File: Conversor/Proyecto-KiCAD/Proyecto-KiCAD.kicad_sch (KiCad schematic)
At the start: 41 parts, among them Q1 IRFP150, Q2 IRFP150, Q3 IRFP150, Q4 IRFP150, U1 UCC21540, U2 UCC21540

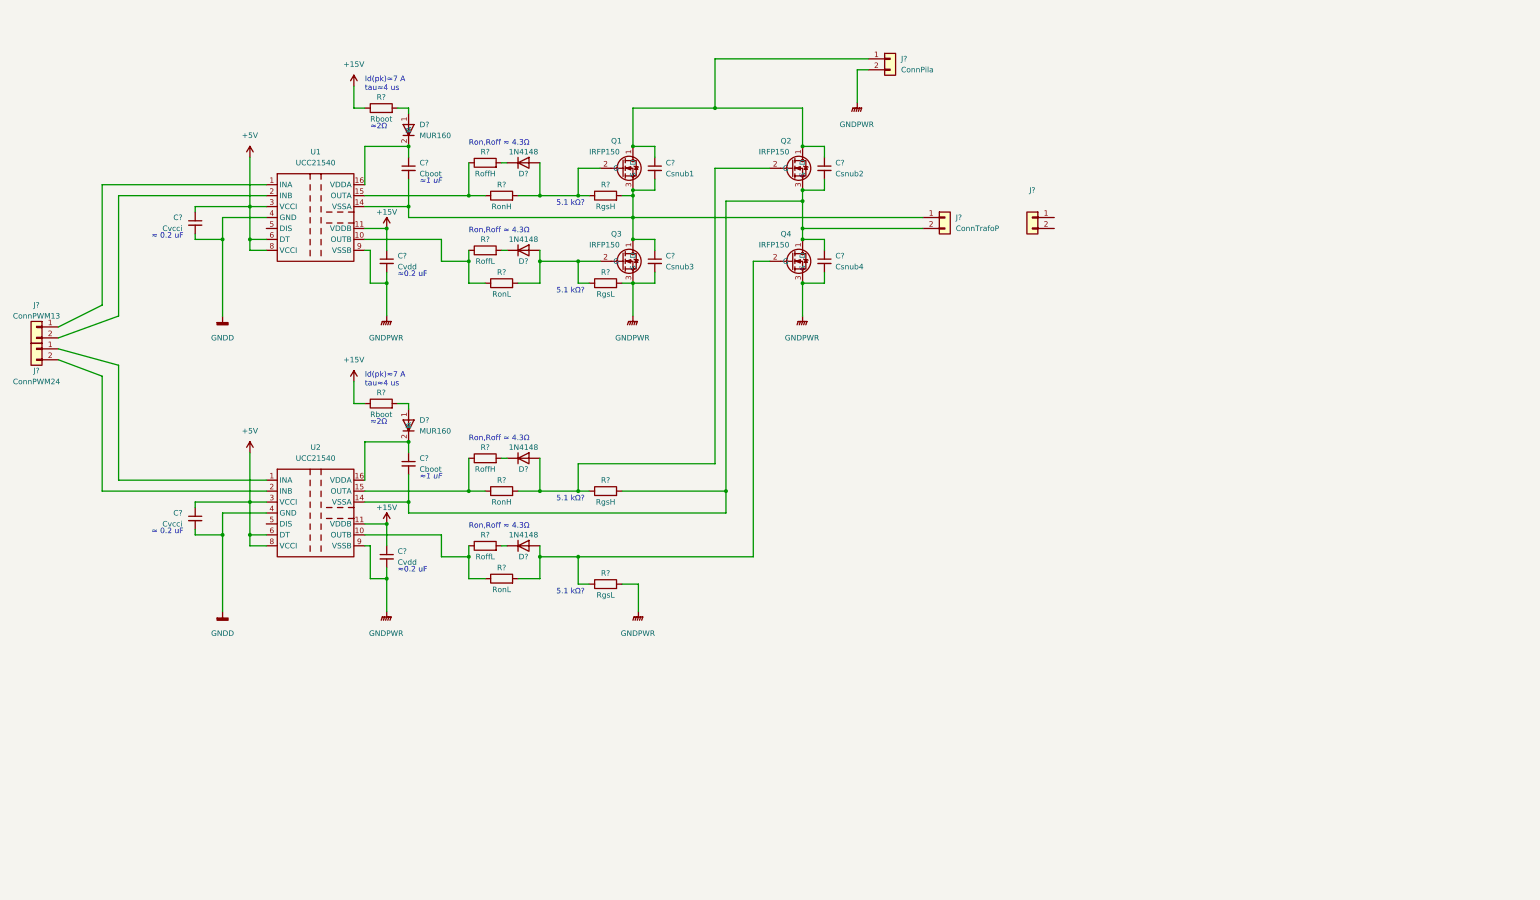
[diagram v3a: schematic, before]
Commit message: Terminar el esquematico del conversor
- Arrancado el esquematico de los sensores de tension/corriente/potencia
- Agregado el sensor Hall (ACS709) a la biblioteca de KiCAD y su datasheet
- Agregada datasheet de diodos MUR860 y SF86
- Mandado mail a Elemon consultando stock de diodos y transistores
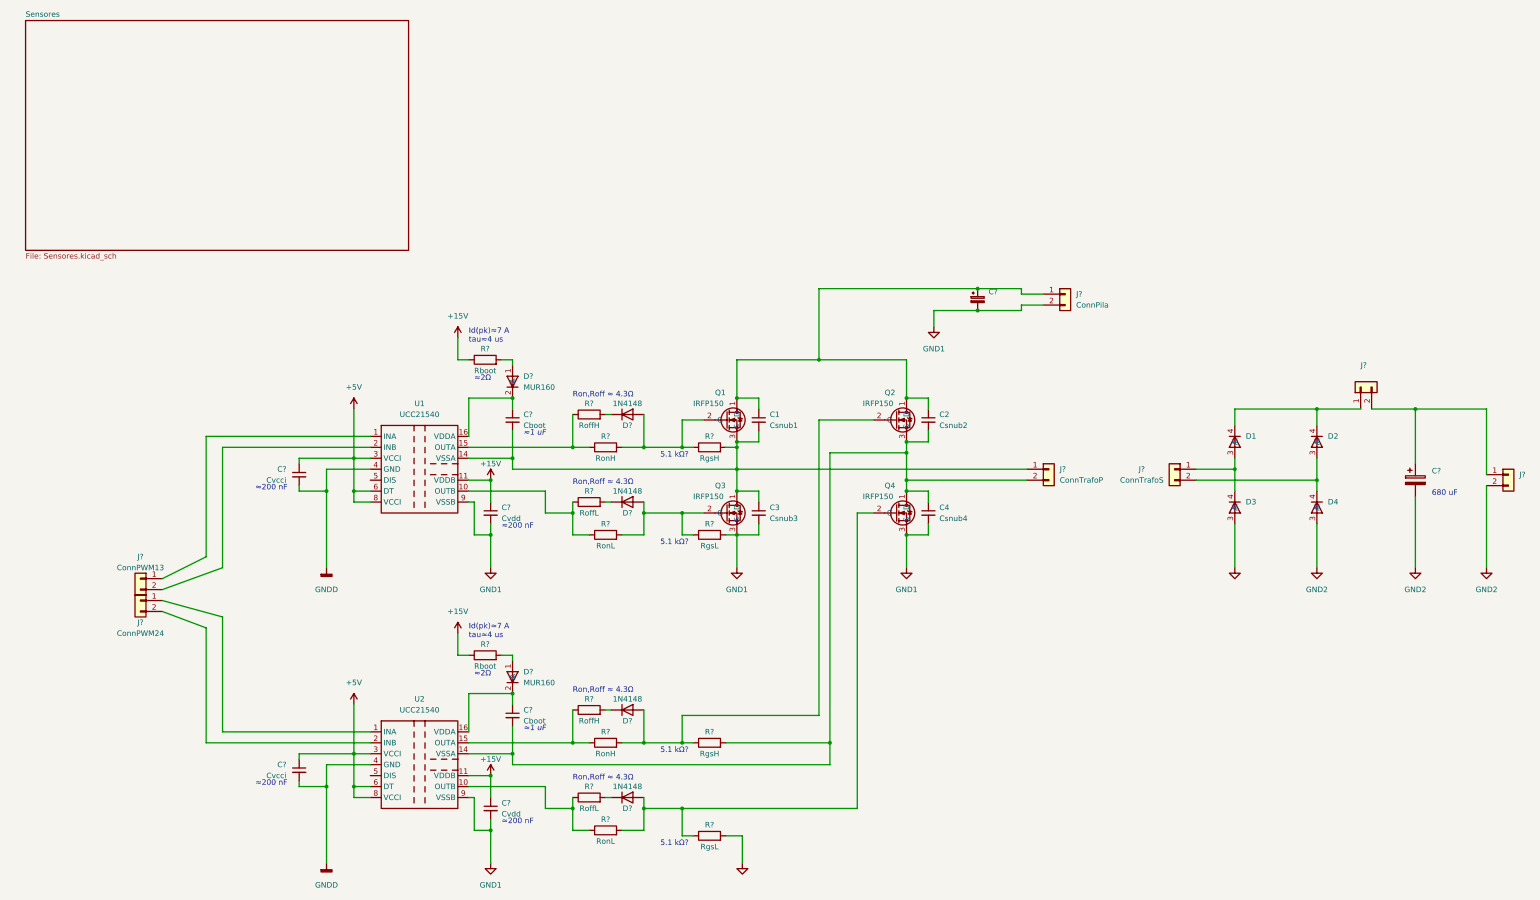
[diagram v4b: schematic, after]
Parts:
- added C?: (no value), symbol Device:C_Polarized
- added C?: (no value), symbol Device:C_Polarized_Small
- added D1, D2, D3, D4: (no value), symbol Componentes proyecto:MUR860
- added J? (x2): (no value), symbol Connector_Generic:Conn_01x02
- J?: value (none) -> ConnTrafoS
- gave numbers to parts that had none: 4
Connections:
- net at C1.1, C2.1, J?.1 (Pin_1)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: now also C?.1
- net at J?.1 (Pin_1): now also D1.3 (A), D3.4 (K)
- net at J?.2 (Pin_2): now also D2.3 (A), D4.4 (K)
- net GNDPWR renamed GND1
- net GND1: now also C?.2
- new net: D1.4 (K), D2.4 (K), J?.1 (Pin_1)
- new net: C?.1, J?.1 (Pin_1), J?.2 (Pin_2)
- new net GND2: C?.2, D3.3 (A), D4.3 (A), J?.2 (Pin_2)
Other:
- added sheet Sensores (Sensores.kicad_sch)
- note added: "680 uF"
- note added: "≈200 nF"
- note removed: "≈ 0.2 uF"
- note removed: "≈0.2 uF"
- moved on the sheet: C1, C2, C3, C4, C?, D?, J?, Q1, Q2, Q3, Q4, R?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

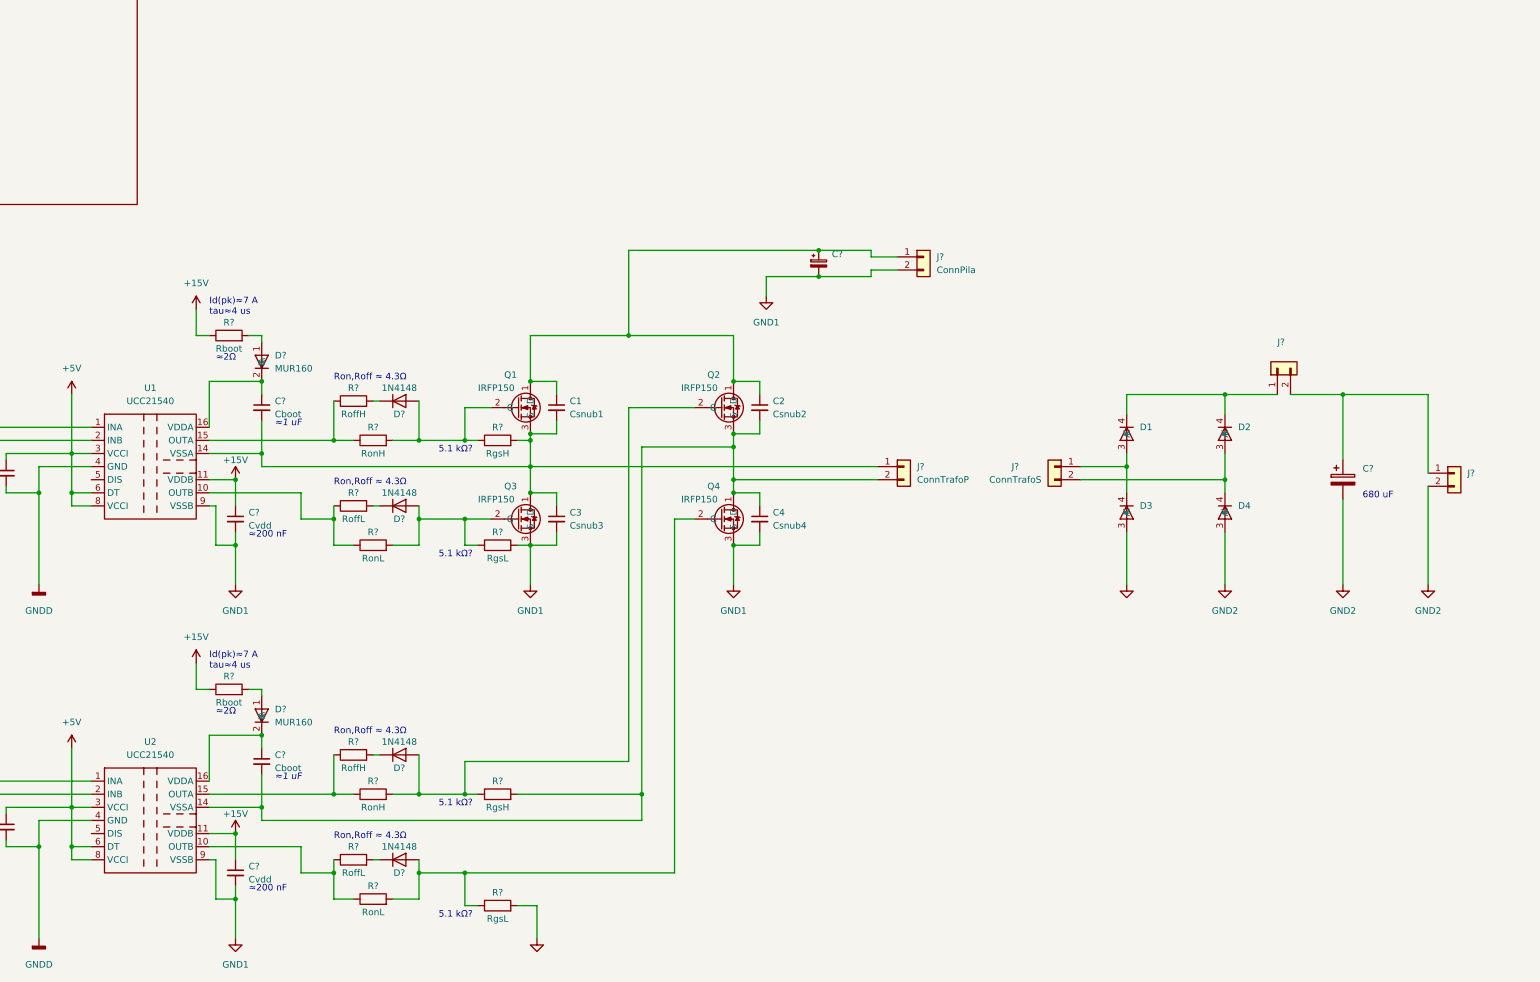
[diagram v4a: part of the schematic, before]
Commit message: Comenzar con la conexion del LM5056A
- Hay que ver el valor de la resistencia shunt RS
- Fijarse si se puede poner los sensores en un archivo distinto
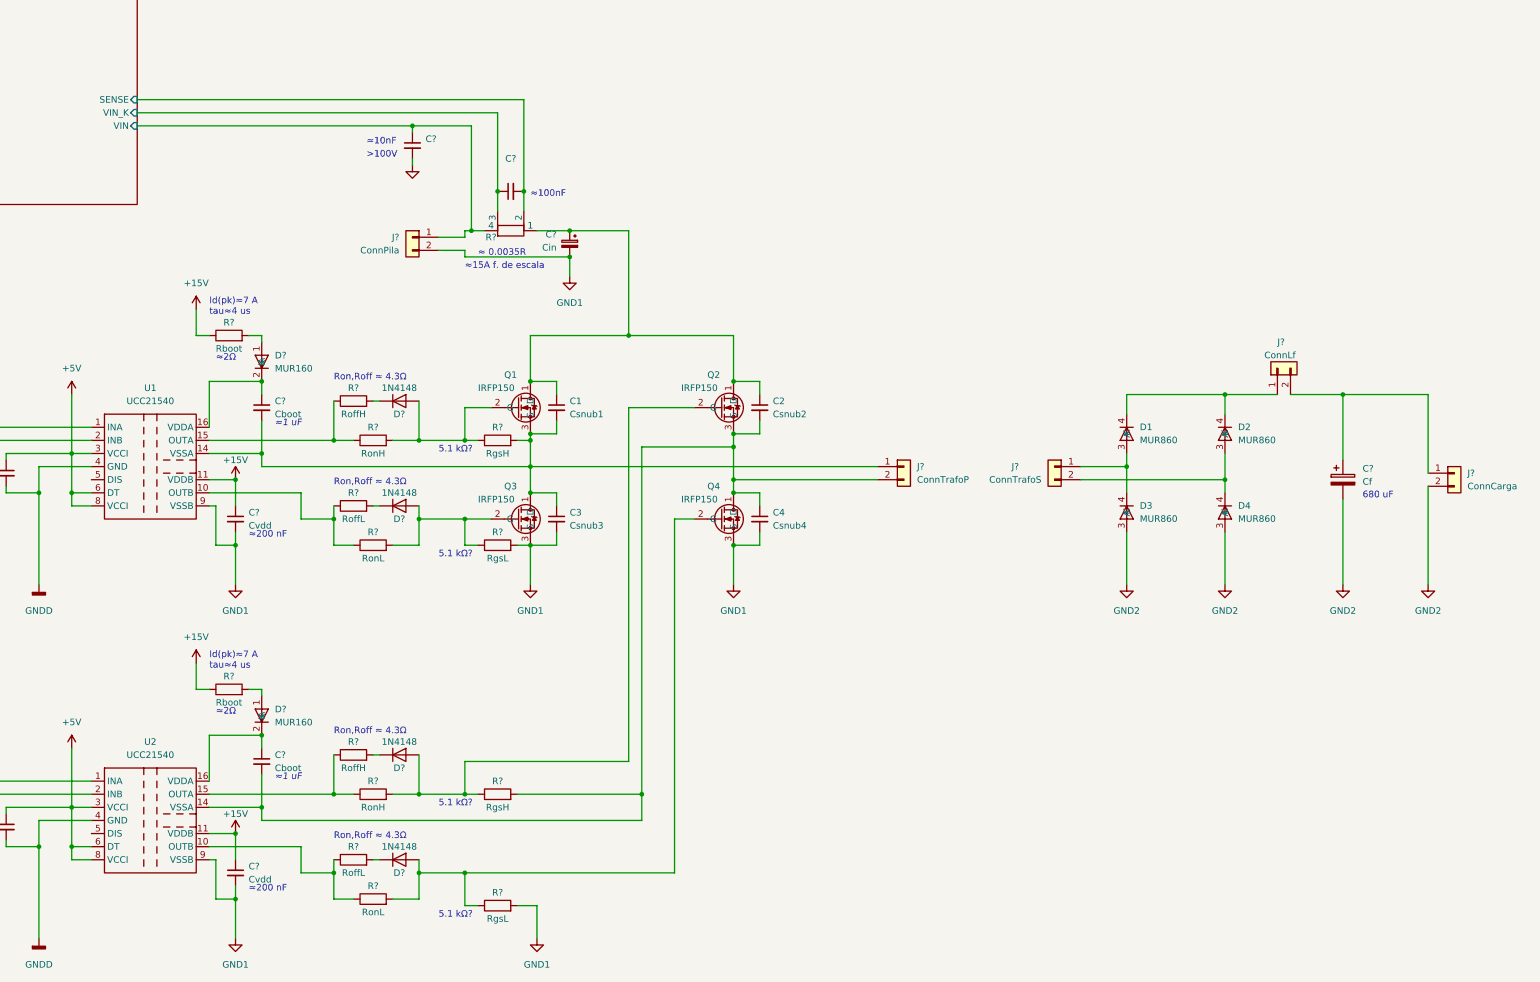
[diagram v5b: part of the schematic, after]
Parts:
- added C? (x2): (no value), symbol Device:C_Small
- added R?: (no value), symbol Device:R_Shunt
- C?: value (none) -> Cf
- C?: value (none) -> Cin
- D1, D2, D3, D4: value (none) -> MUR860
- J?: value (none) -> ConnLf
- J?: value (none) -> ConnCarga
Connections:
- net GND1: now also C?.2
- net at C1.1, C2.1, C?.1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: now also R?.1; no longer J?.1 (Pin_1)
- new net Sensores/SENSE: C?.2, R?.2
- new net Sensores/VIN: C?.1, J?.1 (Pin_1), R?.4
- new net Sensores/VIN_K: C?.1, R?.3
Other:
- sheet Sensores ports: added SENSE, VIN, VIN_K; removed none
- note added: ">100V"
- note added: "≈ 0.0035R"
- note added: "≈100nF"
- note added: "≈10nF"
- note added: "≈15A f. de escala"
- moved on the sheet: C?, J?

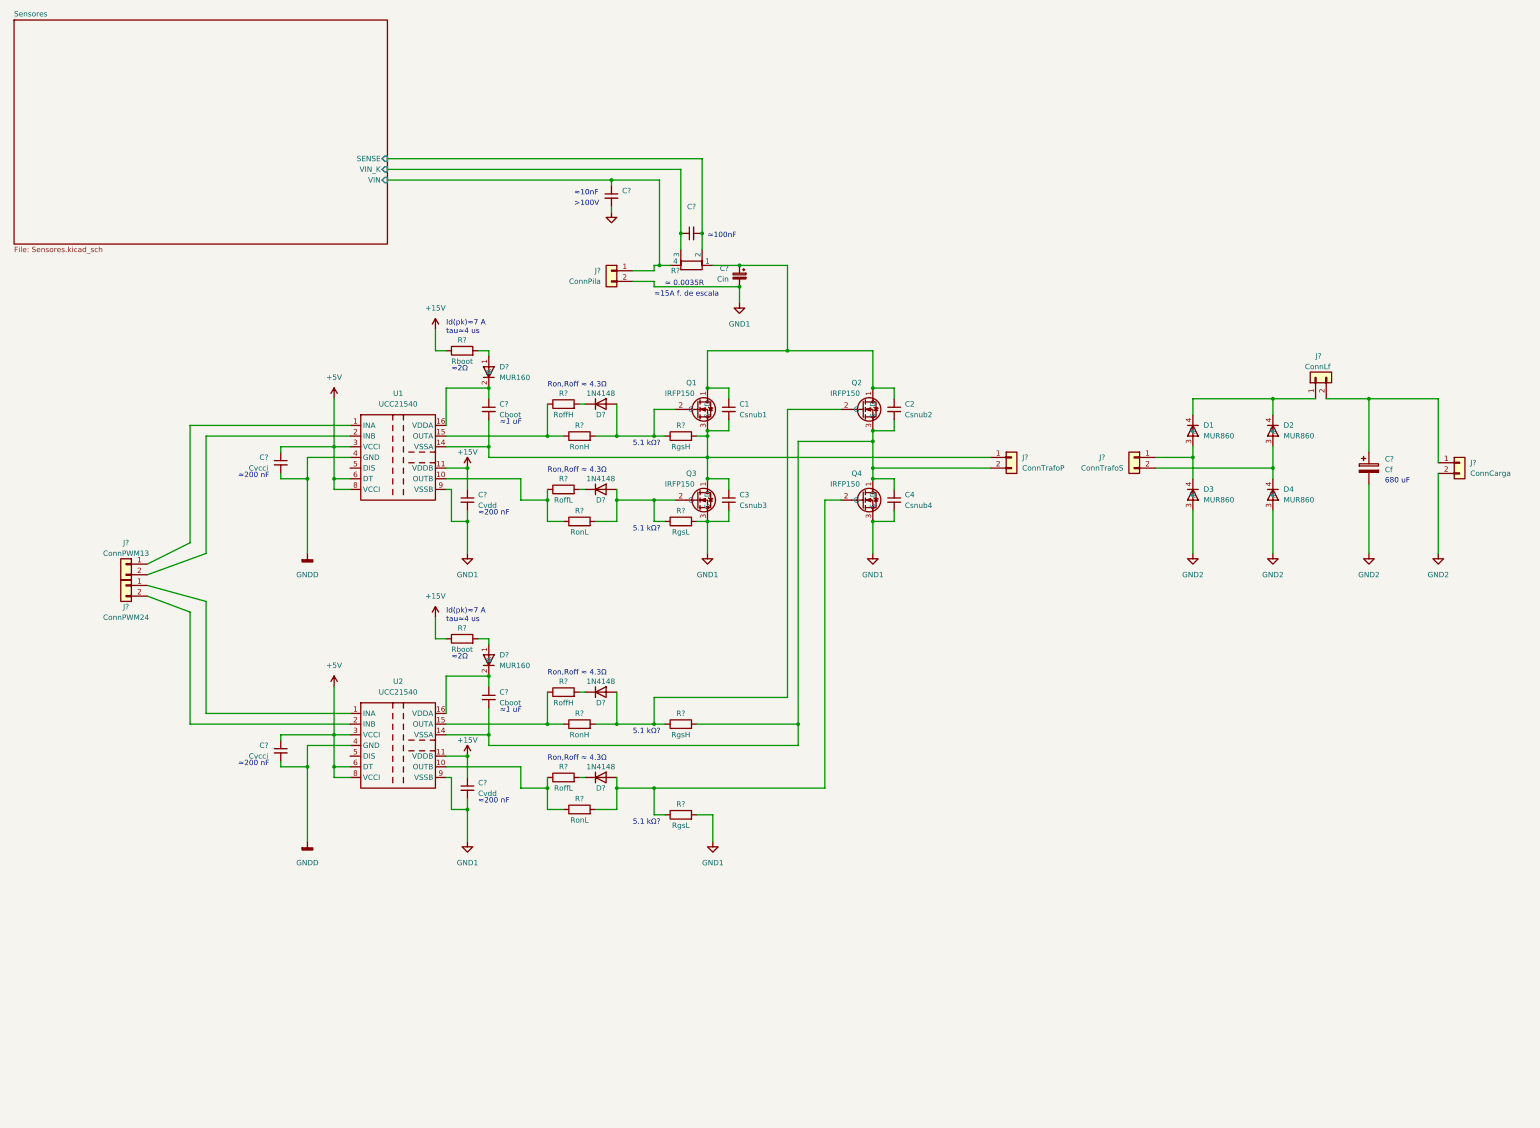
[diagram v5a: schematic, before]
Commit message: Continuar la conexion del esuqematico de sensores
- Agregado y leido un tutorial de I2C de TI
- Pasar de conexiones a la sheet auxiliar -> Global labels
- Aregada la datasheet del DSP que faltaba
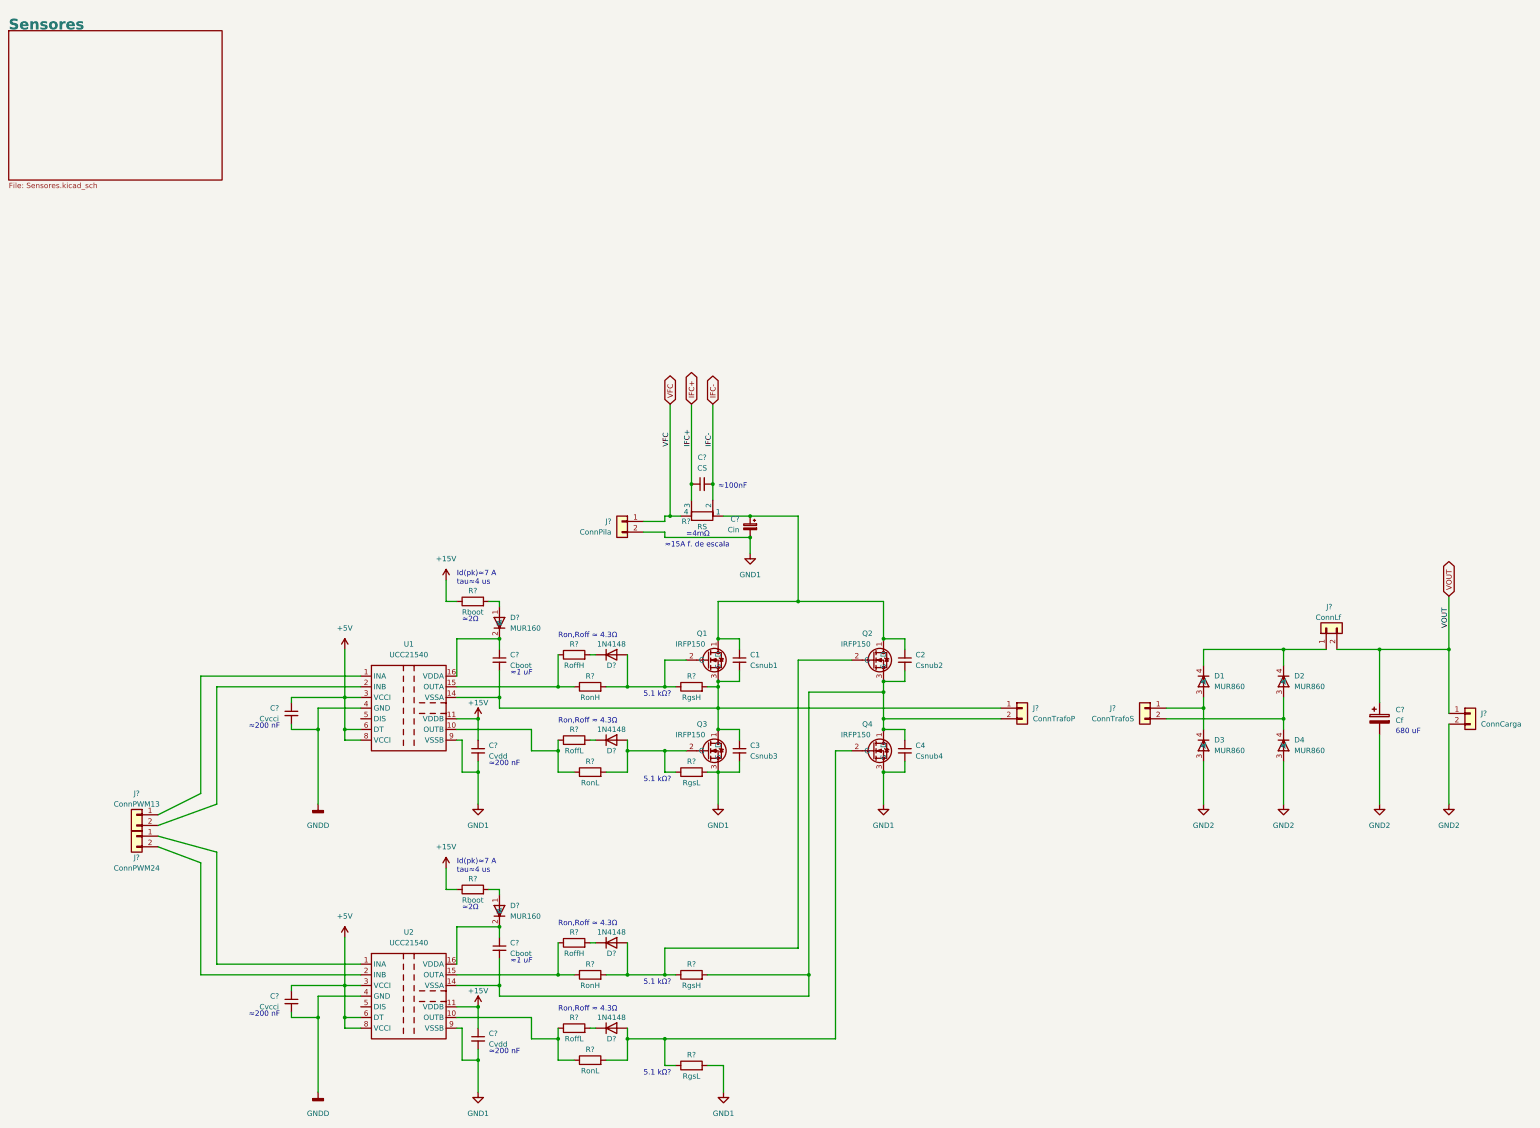
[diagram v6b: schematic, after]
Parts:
- removed C?: (no value), symbol Device:C_Small
- C?: value (none) -> CS
- R?: value (none) -> RS
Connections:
- net VOUT: now reaches C?.1, J?.1 (Pin_1), J?.2 (Pin_2)
- net Sensores/SENSE renamed IFC-
- net Sensores/VIN renamed VFC
- net Sensores/VIN_K renamed IFC+
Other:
- sheet Sensores ports: added none; removed SENSE, VIN, VIN_K
- note added: "=4mΩ"
- note removed: ">100V"
- note removed: "≈ 0.0035R"
- note removed: "≈10nF"
- moved on the sheet: C1, C2, C3, C4, C?, D1, D2, D3, D4, D?, J?, Q1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
